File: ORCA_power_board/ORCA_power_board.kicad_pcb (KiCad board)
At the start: 4 copper layers, 73 x 134.1 mm, 184 parts, among them J1 data_line_power, J10 Raspberry_Pi_2_3, J11 I2C, J12 I2C, J13 6Vout, J15 Conn_01x05_Pin, J16 Conn_01x05_Pin, J17 Vin_motor, J18 data_line_power, J19 +5Vin_cpu, J2 I2C_power, J20 5Vout, J21 Conn_01x02, J3 Vout_motor, J4 emergence, J5 Vin_batt, J6 Vin_ex, J7 Vout_power2usp, J8 Vin_power2usp, J9 +5Vout_cpu, P1 USB_C_Receptacle_USB2.0, Q1 TJ60S04M3L, Q2 BSS138, Q3 BSS138, Q4 IRLML6402, Q5 TJ60S04M3L, Q6 BSS138, Q7 BSS138, Q8 BSS138, U1 LTC2301IMS, U10 HY2112, U11 AP64502, U12 TPS61230A__board, U13 FT230XS, U14 BNO055, U15 NJM78055DL1, U2 NJM78055DL1, U3 CN3058E, U4 RH1B-UDC6V, U5 TPH11006NL, U6 TPH11006NL, U7 NJW4860, U8 AZ1117-3.3, U9 FS8205

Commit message: fixed most of the error. waiting check
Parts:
- removed C40, C46, C47: 4.7u, Capacitor_SMD:C_0603_1608Metric_Pad1.08x0.95mm_HandSolder
- removed C44, C48: 1u, Capacitor_SMD:C_0805_2012Metric_Pad1.18x1.45mm_HandSolder
- removed C45: 0.1u, Capacitor_SMD:C_0603_1608Metric_Pad1.08x0.95mm_HandSolder
- removed C49: 1u/50V, Capacitor_SMD:C_0805_2012Metric_Pad1.18x1.45mm_HandSolder
- removed C50: 0.1u25V, Capacitor_SMD:C_0603_1608Metric_Pad1.08x0.95mm_HandSolder
- removed D19: LED_cpu, LED_SMD:LED_0603_1608Metric_Pad1.05x0.95mm_HandSolder
- removed D20: LED_motor, LED_SMD:LED_0603_1608Metric_Pad1.05x0.95mm_HandSolder
- removed D22, D25: CUHS20560, Diode:Diode_US2H
- removed D23: LED_usb, LED_SMD:LED_0603_1608Metric_Pad1.05x0.95mm_HandSolder
- removed D24: WS2812B, LED_SMD:LED_WS2812B_PLCC4_5.0x5.0mm_P3.2mm
- removed H10: Hole_cup, MountingHole:MountingHole_3.2mm_M3
- removed H9: Hole_cpu, MountingHole:MountingHole_3.2mm_M3
- removed J10: Raspberry_Pi_2_3, cpu:raspberrypi_Zero_W_Vertical
- removed J11, J12: I2C, Connector_JST:JST_XH_B3B-XH-A_1x03_P2.50mm_Vertical
- removed J13: 6Vout, Conn:power_pad
- removed J15, J16: Conn_01x05_Pin, Connector_PinHeader_2.54mm:PinHeader_1x05_P2.54mm_Vertical
- removed J17: Vin_motor, Conn:power_pad
- removed J18: data_line_power, Connector_JST:JST_XH_B3B-XH-A_1x03_P2.50mm_Vertical
- removed J19: +5Vin_cpu, Conn:power_pad
- removed J20: 5Vout, Conn:power_pad
- removed the ORCA_CORE at (106.0, 46.4)
- removed P1: USB_C_Receptacle_USB2.0, Conn:USB_C_Receptacle_XKB_U262-16XN-4BVC11
- removed Q6, Q7, Q8: BSS138, Package_TO_SOT_SMD:SOT-23
- removed R34, R37, R38, R41, R42, R43, R44, R45, R46, R47, R48, R49, R6: 2.2k, Resistor_SMD:R_0603_1608Metric_Pad0.98x0.95mm_HandSolder
- removed R35, R36, R40: 1k, Resistor_SMD:R_0603_1608Metric_Pad0.98x0.95mm_HandSolder
- removed R39, R51: 5.1k, Resistor_SMD:R_0603_1608Metric_Pad0.98x0.95mm_HandSolder
- removed U13: FT230XS, Package_SO:SSOP-16_3.9x4.9mm_P0.635mm
- removed U14: BNO055, IMU:BNO055
- removed U15: NJM78055DL1, Package_TO_SOT_SMD:TO-252-2
- Q4: value IRLML6402 -> BSS138
- R13: value 4.7k -> 4.7
- R25: value 47k -> 22k
- R26: value 4.7k -> 22k
- R27: value 510 -> 2k
- R33: value 10k -> 4.7
- U1: footprint Package_DFN_QFN:TDFN-12_2x3mm_P0.5mm -> Package_SO:MSOP-12_3x4mm_P0.65mm
- U3: footprint Package_SO:TSSOP-8_3x3mm_P0.65mm -> Package_SO:HTSOP-8-1EP_3.9x4.9mm_P1.27mm_EP2.4x3.2mm
- U9: footprint Package_TO_SOT_SMD:TSOT-23-6_HandSoldering -> Package_SO:TSSOP-8_4.4x3mm_P0.65mm
- moved R7 26.5 mm to (125.8, 120.8)
- moved U1 25.9 mm to (126.4, 110.8)
- moved C7 25.4 mm to (122.4, 117.0)
- moved U6 25.3 mm to (158.9, 122.8)
- moved U2 25.2 mm to (124.3, 118.7)
- moved C16 25.1 mm to (163.9, 113.3)
- moved F1 25.1 mm to (134.1, 115.0)
- moved D3 25.1 mm to (139.2, 119.2)
- moved C18 25.1 mm to (150.6, 132.4)
- moved C20 25.1 mm to (122.7, 130.3)
- moved C25 25.1 mm to (116.6, 62.2)
- moved C30 25.1 mm to (151.2, 77.5)
- moved C31 25.1 mm to (147.7, 84.2)
- moved C34 25.1 mm to (145.8, 84.2)
- moved C36 25.1 mm to (139.1, 75.4)
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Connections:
- J2 pad 1: VBUS_power -> +3V3_power
- Q1 pad 1: +BATT_power -> Net-(D14-K)
- Q1 pad 3: Net-(D14-K) -> +BATT_power
- Q2 pad 1: VBUS_power -> +3V3_power
- Q3 pad 1: VBUS_power -> +3V3_power
- Q4 pad 1: +6V_power -> /power/Vout_motor
- R11 pad 2: +6V_power -> /power/Vout_motor
- R13 pad 1: Net-(Q1-G) -> +VDD_power
- R13 pad 2: +VDD_power -> Net-(Q1-G)
- R7 pad 1: VBUS_power -> +3V3_power
- R9 pad 1: VBUS_power -> +3V3_power
- U2 pad 1: GND -> +6V_power
- U2 pad 2: +5V_power -> GND
- U2 pad 3: +6V_power -> +5V_power
- U5 pad 1: Net-(D6-K) -> GND
- U5 pad 2: Net-(D6-K) -> GND
- U5 pad 3: Net-(D6-K) -> GND
- U5 pad 5: GND -> Net-(D6-K)
- U5 pad 6: GND -> Net-(D6-K)
- U5 pad 7: GND -> Net-(D6-K)
- U5 pad 8: GND -> Net-(D6-K)
- U6 pad 1: Net-(D8-K) -> GND
- U6 pad 2: Net-(D8-K) -> GND
- U6 pad 3: Net-(D8-K) -> GND
- U6 pad 5: GND -> Net-(D8-K)
- U6 pad 6: GND -> Net-(D8-K)
- U6 pad 7: GND -> Net-(D8-K)
- U6 pad 8: GND -> Net-(D8-K)
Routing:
- net GND2: track 147.3 -> 0.00 mm, vias 48 -> 0
- net SCL: track 76.7 -> 0.00 mm, vias 1 -> 0
- net SDA: track 74.9 -> 0.00 mm, vias 4 -> 0
- net +5V_cpu: track 64.6 -> 0.00 mm, vias 19 -> 0
- net +3V3_cpu: track 62.8 -> 0.00 mm, vias 9 -> 0
- net full_color_led_3V3: track 54.1 -> 0.00 mm
- net /cpu/GPIO21: track 51.4 -> 0.00 mm
- net /cpu/GPIO20: track 50.9 -> 0.00 mm, vias 3 -> 0
- net /cpu/GPIO19: track 50.6 -> 0.00 mm, vias 3 -> 0
- net +3V3_power: track 46.4 -> 93.5 mm
- net batt+: track 62.2 -> 16.0 mm
- net /cpu/GPIO26: track 44.7 -> 0.00 mm, vias 1 -> 0
- net /cpu/GPIO16: track 44.6 -> 0.00 mm, vias 3 -> 0
- net /cpu/GPIO12: track 43.2 -> 0.00 mm, vias 3 -> 0
- net RXD_3V3: track 41.9 -> 0.00 mm, vias 1 -> 0
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- removed copper zone on In1.Cu, net +3V3_cpu
- removed copper zone on B.Cu, net +5V_cpu
- removed copper zone on F.Cu, net +5V_cpu
- removed copper zone on In1.Cu, net +5V_cpu
- removed copper zone on In2.Cu, net +5V_cpu
- removed copper zone on B.Cu, net +5V_cpu2servo
- removed copper zone on In1.Cu, net +5V_cpu2servo
- removed copper zone on B.Cu, net +6V_cpu
- removed copper zone on F.Cu, net +6V_cpu
- removed copper zone on In1.Cu, net +6V_cpu
- removed copper zone on B.Cu, net GND2
- removed copper zone on F.Cu, net GND2
- removed copper zone on In2.Cu, net GND2
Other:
- board size 73 x 134.1 mm -> 73 x 86.2 mm
- board text removed: "12"
- board text removed: "13"
- board text removed: "16"
- board text removed: "17"
- board text removed: "18"
- board text removed: "19"
- board text removed: "20"
- board text removed: "21"
- board text removed: "26"
- board text removed: "27"
- board text removed: "Vin_5Vcpu"
- board text removed: "Vout 5V_motor"
- board text removed: "Vout 6V"
- board text removed: "cpu board v1 2025/02/19"

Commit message: complete power_board
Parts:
- J8: footprint Conn:power_pad -> Conn:AMASS_XT30U-F_Vertical_withmodel_female; moved to B.Cu
- J9: footprint Conn:power_pad -> Conn:AMASS_XT30U-F_Vertical_withmodel_male; moved to B.Cu
- U9: value FS8205 -> FS8205A
- moved C25 4.54 mm to (116.6, 66.8)
- moved J8 4.52 mm to (109.1, 85.8)
- moved U9 4.33 mm to (164.6, 68.1)
- moved D10 4.19 mm to (110.2, 70.9)
- moved ORCA_CORE 4.19 mm to (115.6, 79.8)
- moved Q5 4.19 mm to (117.2, 76.3)
- moved R22 4.19 mm to (110.1, 72.8)
- moved R24 4.19 mm to (151.3, 73.4)
- moved R27 4.19 mm to (158.9, 73.4)
- moved R28 4.19 mm to (155.0, 73.4)
- moved R33 4.19 mm to (123.3, 81.7)
- moved C35 4.19 mm to (160.4, 63.4)
- moved R30 4.19 mm to (157.4, 63.4)
- moved U10 4.19 mm to (165.3, 63.3)
- moved C24 4.19 mm to (121.3, 63.0)
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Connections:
- Q5 pad 1: batt+ -> reg_up
- Q5 pad 3: reg_up -> batt+
- U3 pad 9: (no net) -> GND
- U9 pad 1: batt- -> unconnected-(U9-Pad1)
- U9 pad 2: unconnected-(U9-Pad2) -> GND
- U9 pad 5: unconnected-(U9-Pad5) -> Net-(U10-OD)
- U9 pad 6: Net-(U10-OD) -> batt-
- U9 pad 7: (no net) -> batt-
- U9 pad 8: (no net) -> unconnected-(U9-Pad8)
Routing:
- net batt+: track 16.0 -> 82.0 mm, vias 0 -> 4
- net Net-(Q5-G): track 6.14 -> 20.4 mm, vias 0 -> 2
- net GND: track 65.2 -> 75.5 mm, vias 161 -> 181
- net batt-: track 12.9 -> 20.6 mm
- net +VDD_usp: track 34.8 -> 42.4 mm
- net Net-(D12-K): track 8.43 -> 15.3 mm
- net +VDD_power: track 16.1 -> 10.6 mm
- net Net-(U3-ISET): track 4.39 -> 8.77 mm, vias 0 -> 2
- net Net-(D10-K): track 6.99 -> 11.3 mm, vias 0 -> 1
- net Net-(U10-OC): track 13.8 -> 17.9 mm, vias 2 -> 0
- net reg_up: track 11.7 -> 13.7 mm
- net Net-(Q1-G): track 12.0 -> 11.1 mm
- net reg_down_out: vias 38 -> 53
- net Net-(D14-K): vias 4 -> 28
- net /usp/Vin: vias 8 -> 17
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- added copper zone on B.Cu, net Net-(D14-K)
- added copper zone on In2.Cu, net Net-(D14-K)
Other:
- board size 73 x 86.2 mm -> 73 x 82 mm

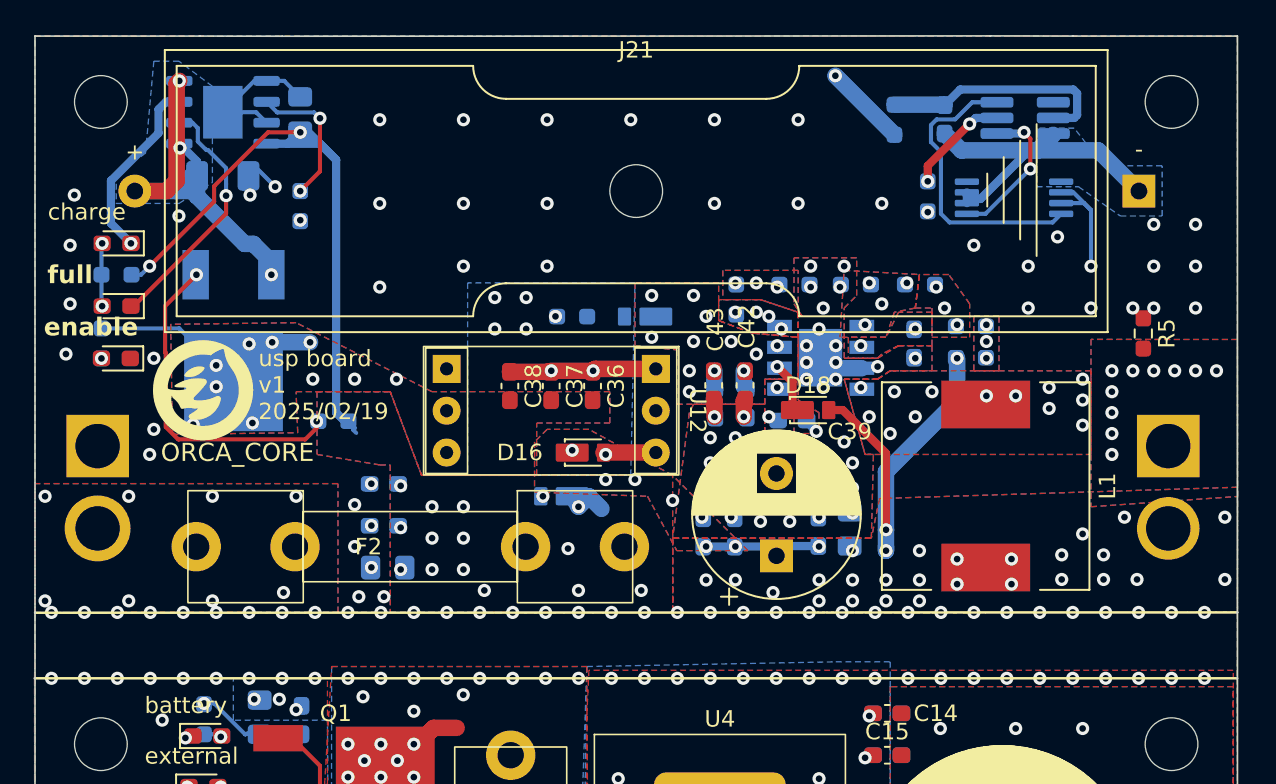
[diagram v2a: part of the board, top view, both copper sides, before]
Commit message: ordered power board
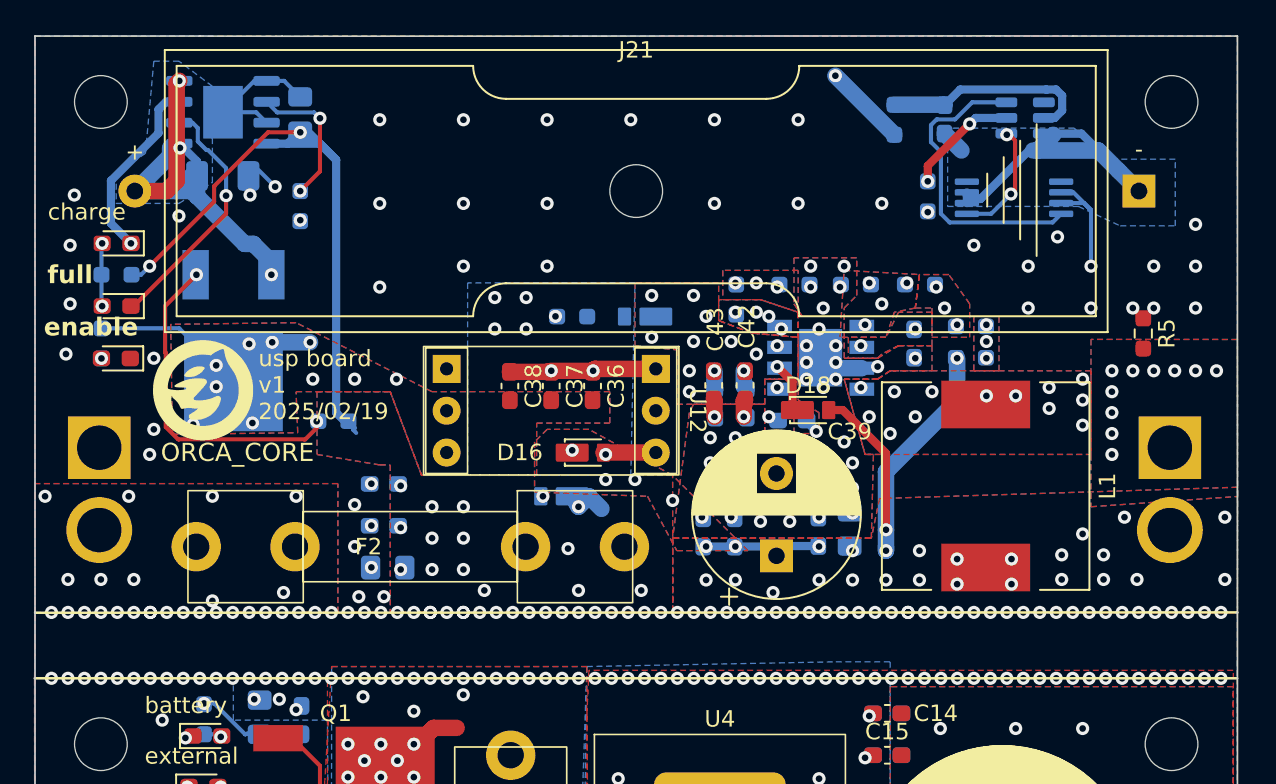
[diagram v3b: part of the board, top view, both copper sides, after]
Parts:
- J8: footprint Conn:AMASS_XT30U-F_Vertical_withmodel_female -> Connector_AMASS:AMASS_XT30U-F_1x02_P5.0mm_Vertical
- J9: footprint Conn:AMASS_XT30U-F_Vertical_withmodel_male -> Connector_AMASS:AMASS_XT30U-F_1x02_P5.0mm_Vertical
- U10: footprint Package_TO_SOT_SMD:TSOT-23-6_HandSoldering -> Package_TO_SOT_SMD:TSOT-23-6
- moved J8 2.50 mm to (109.1, 83.3)
- moved J9 2.50 mm to (174.1, 83.3)
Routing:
- net batt+: track 82.0 -> 85.5 mm
- net Net-(U10-OD): track 9.04 -> 7.32 mm
- net Net-(U10-VDD): track 14.4 -> 12.9 mm
- net batt-: track 20.6 -> 21.1 mm
- net reg_down_out: vias 53 -> 67
- net Net-(D14-K): vias 28 -> 35
- net GND: vias 181 -> 187
- net /usp/Vin: vias 17 -> 27
- net /power/Vout_motor: vias 35 -> 45
- net +VDD_usp: vias 20 -> 39
- net +BATT_power: vias 17 -> 23

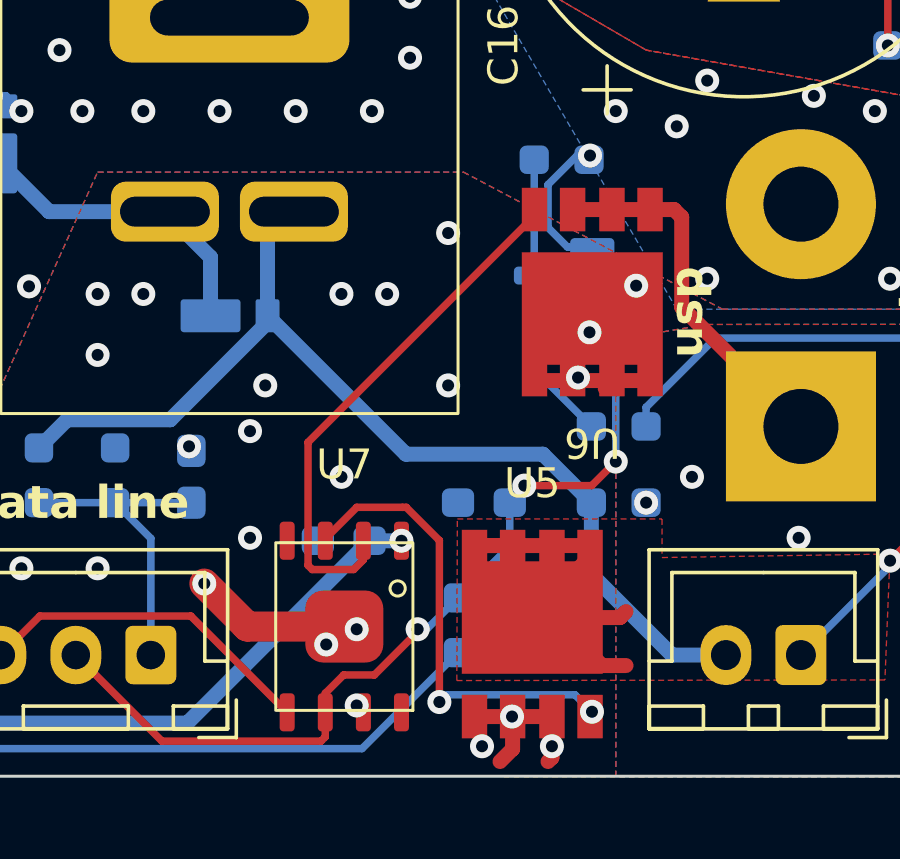
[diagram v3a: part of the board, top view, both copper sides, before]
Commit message: add power registers to power_board gate driver
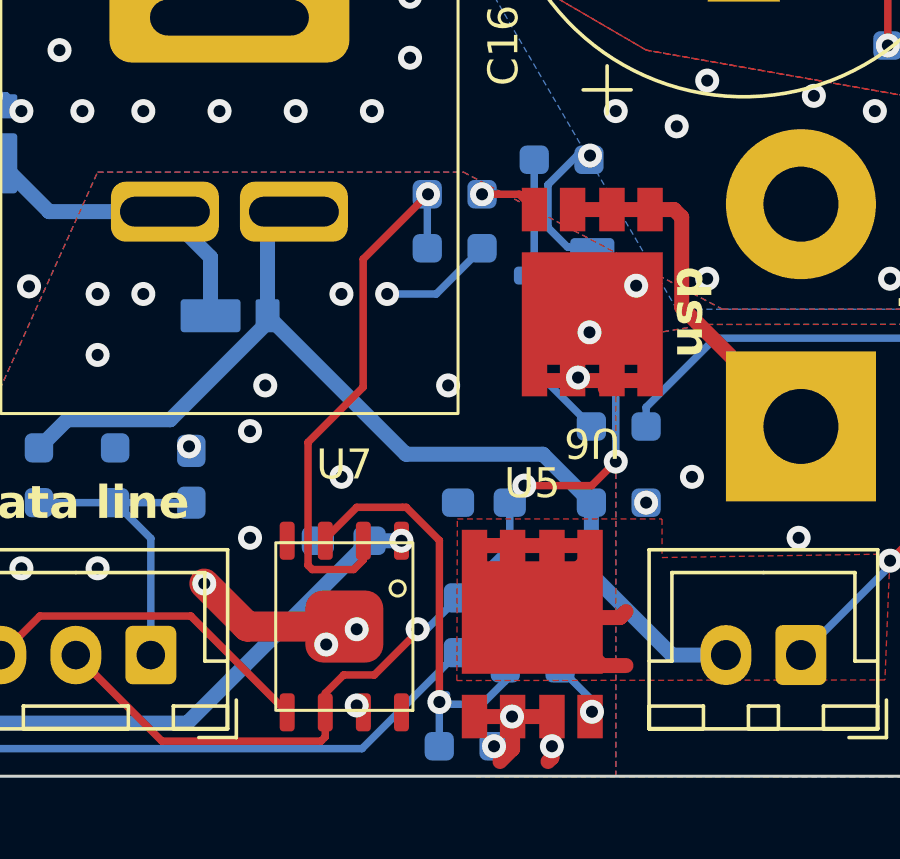
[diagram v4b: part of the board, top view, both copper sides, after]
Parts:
- added R34: 22, Resistor_SMD:R_0603_1608Metric_Pad0.98x0.95mm_HandSolder, B.Cu at (154.3, 120.9)
- added R35: 2.2k, Resistor_SMD:R_0603_1608Metric_Pad0.98x0.95mm_HandSolder, B.Cu at (154.3, 122.7)
- added R36: 2.2k, Resistor_SMD:R_0603_1608Metric_Pad0.98x0.95mm_HandSolder, B.Cu at (154.7, 139.3)
- added R6: 22, Resistor_SMD:R_0603_1608Metric_Pad0.98x0.95mm_HandSolder, B.Cu at (156.9, 136.7)
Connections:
- U5 pad 4: Net-(U7-OUTB) -> Net-(R6-Pad2)
- U6 pad 4: Net-(U7-OUTA) -> Net-(R34-Pad2)
- U7 pad 3: Net-(U7-OUTB) -> Net-(U7-OUTA)
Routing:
- net Net-(U7-OUTB): track 16.2 -> 0.00 mm, vias 2 -> 0
- net Net-(U7-OUTA): track 17.4 -> 33.5 mm, vias 0 -> 2
- net GND: track 75.5 -> 79.3 mm, vias 187 -> 186
- net Net-(R6-Pad2): track 0.00 -> 2.47 mm, vias 0 -> 1
- net Net-(R34-Pad2): track 0.00 -> 1.76 mm, vias 0 -> 1

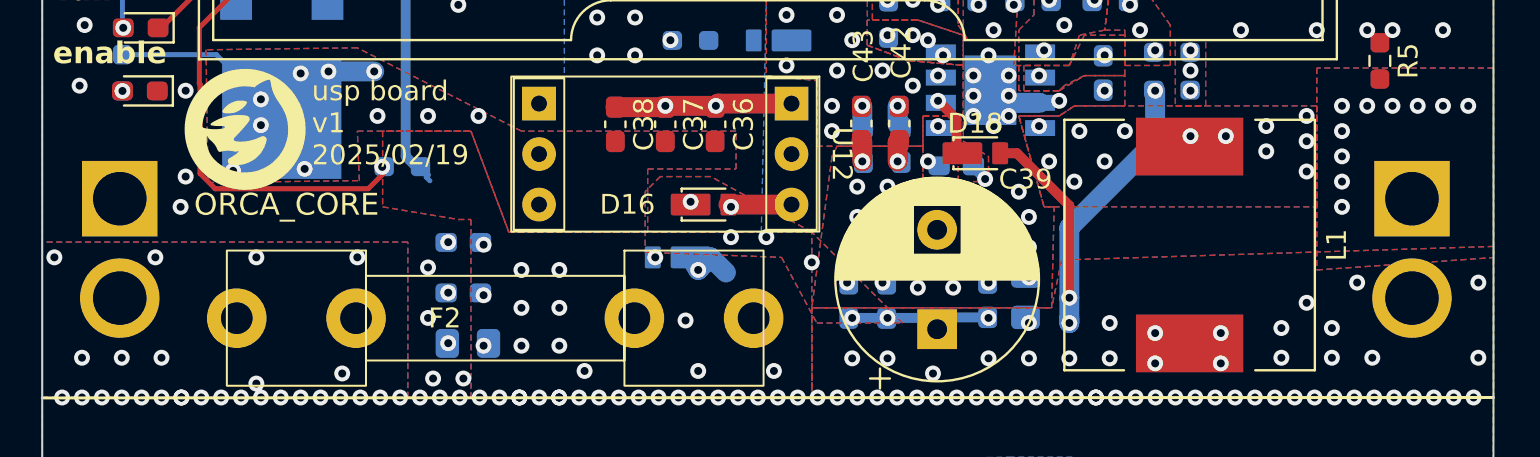
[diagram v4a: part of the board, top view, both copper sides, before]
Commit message: correct few errors in usp
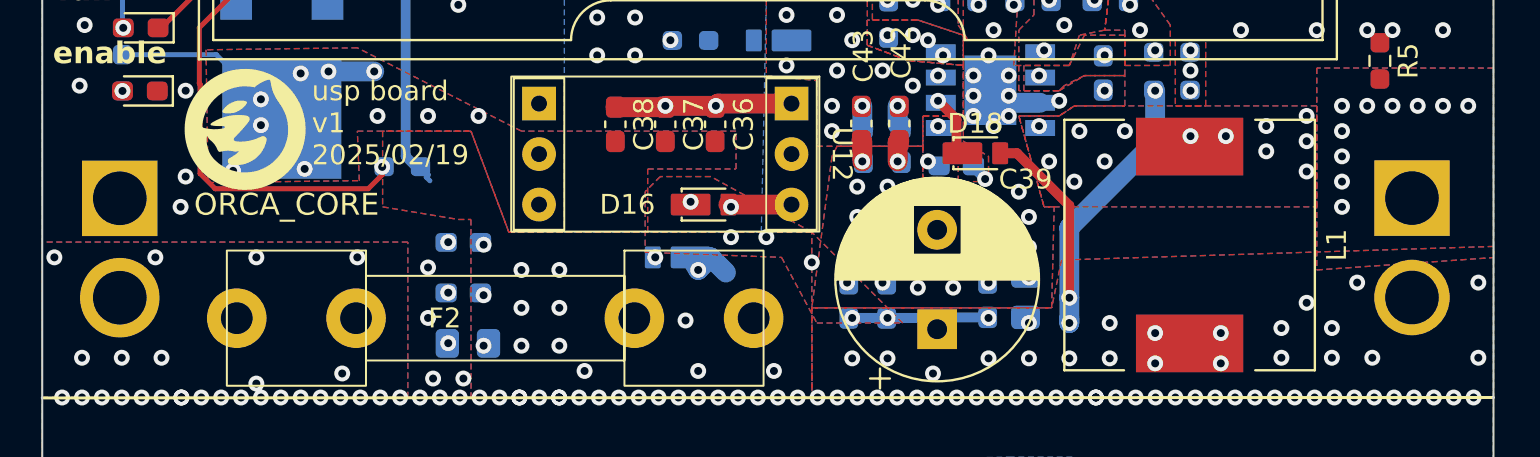
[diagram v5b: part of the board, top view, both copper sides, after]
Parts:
- J8: footprint Connector_AMASS:AMASS_XT30U-F_1x02_P5.0mm_Vertical -> Conn:AMASS_XT30U-F_Vertical_withmodel_female
- J9: footprint Connector_AMASS:AMASS_XT30U-F_1x02_P5.0mm_Vertical -> Conn:AMASS_XT30U-F_Vertical_withmodel_male
- moved J8 2.58 mm to (109.2, 85.9)
- moved J9 2.57 mm to (174.2, 85.9)
